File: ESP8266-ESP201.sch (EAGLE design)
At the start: 17 parts

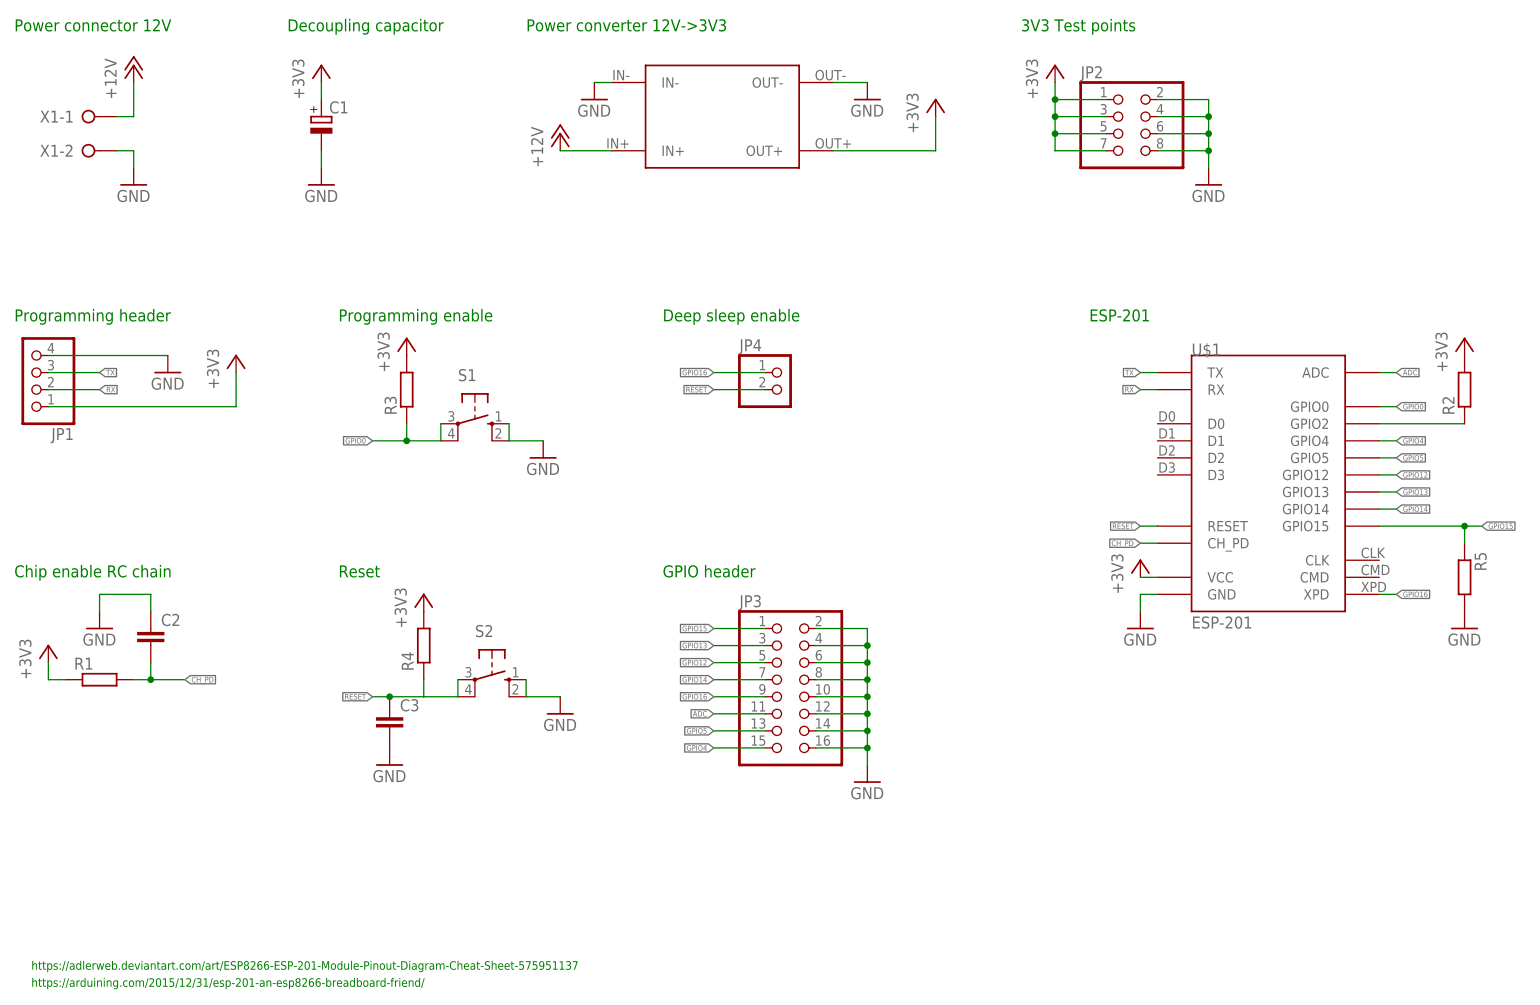
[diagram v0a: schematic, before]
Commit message: New version of the board with proper mounting holes and smaller footprint
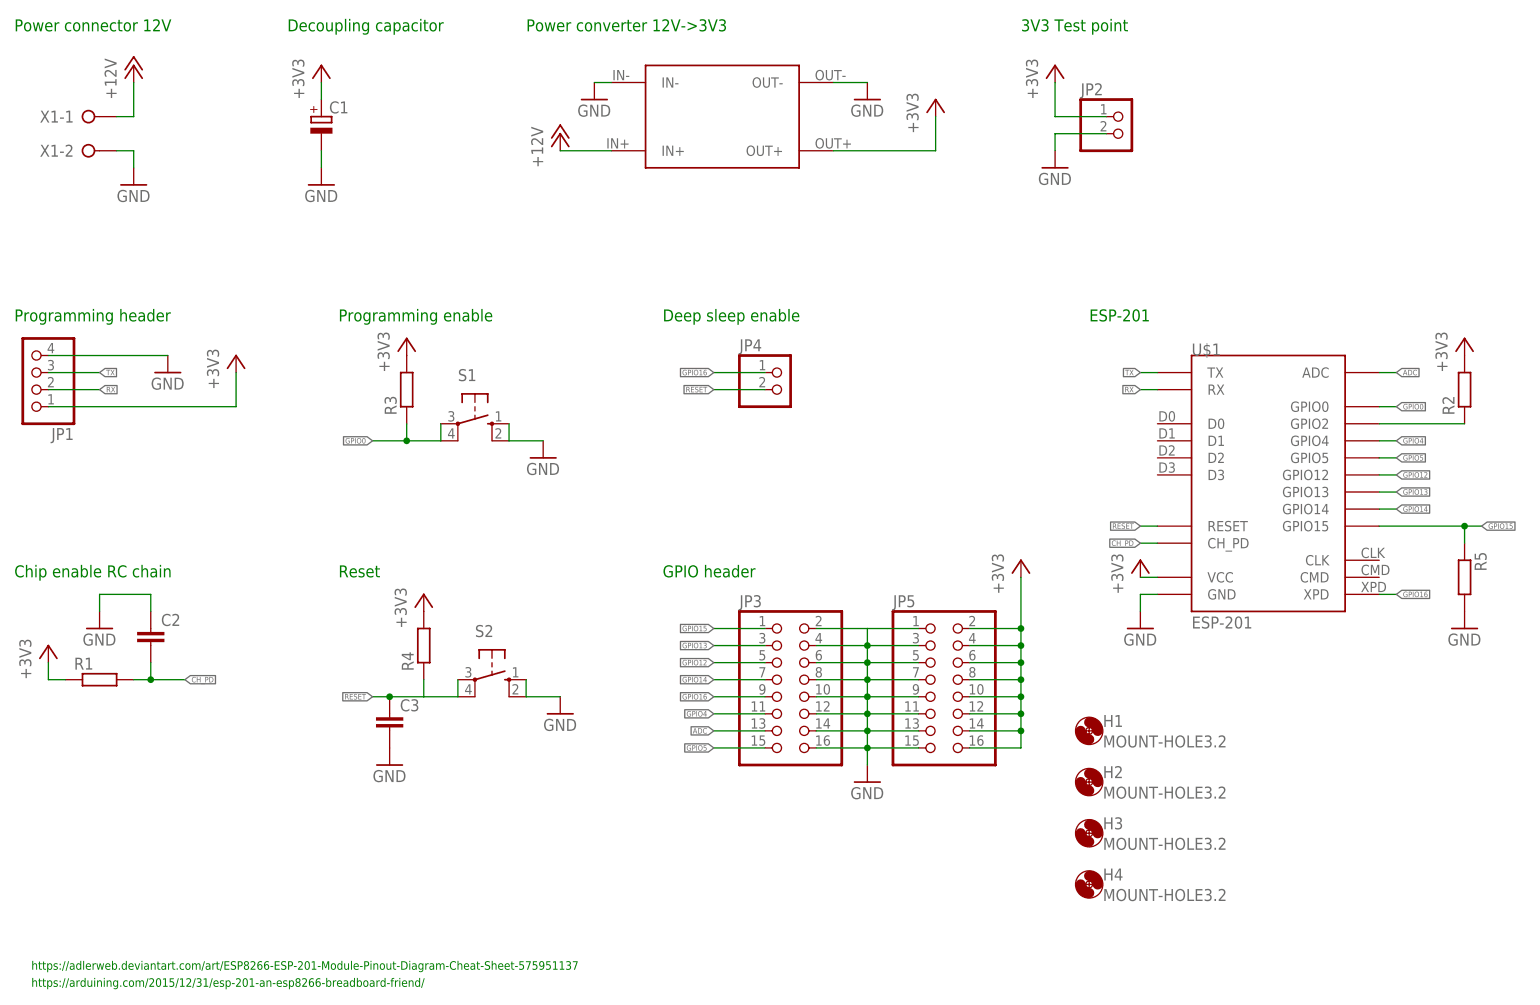
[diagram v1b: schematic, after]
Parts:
- added H1, H2, H3, H4: MOUNT-HOLE3.2, holes:MOUNT-HOLE3.2
- added JP5: (no value), pinhead:PINHD-2X8
- JP2: device pinhead:PINHD-2X4 -> pinhead:PINHD-1X2
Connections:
- net +3V3: now also JP5.10, JP5.12, JP5.14, JP5.16, JP5.2, JP5.4, JP5.6, JP5.8; no longer JP2.3, JP2.5, JP2.7
- net ADC: now also JP3.13; no longer JP3.11
- net GND: now also JP5.1, JP5.11, JP5.13, JP5.15, JP5.3, JP5.5, JP5.7, JP5.9; no longer JP2.4, JP2.6, JP2.8
- net GPIO4: now also JP3.11; no longer JP3.15
- net GPIO5: now also JP3.15; no longer JP3.13
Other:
- note added: "3V3 Test point"
- note removed: "3V3 Test points"

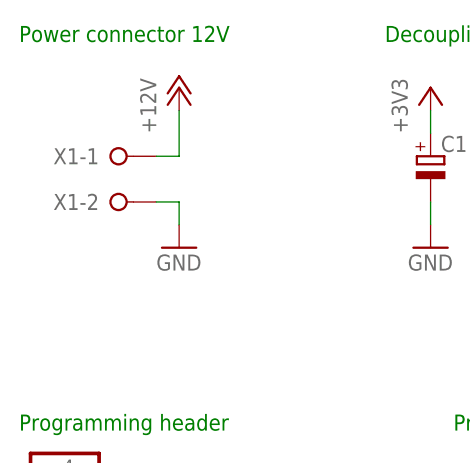
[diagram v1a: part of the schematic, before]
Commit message: More compact layout and added bottom silk screen
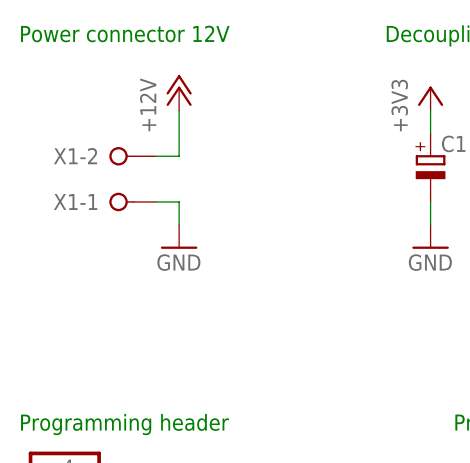
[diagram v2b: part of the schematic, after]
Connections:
- net +12V: now also X1-2.KL; no longer X1-1.KL
- net GND: now also X1-1.KL; no longer X1-2.KL
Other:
- moved on the sheet: X1-1, X1-2
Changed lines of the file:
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@@
 <?xml version="1.0" encoding="utf-8"?>
 <!DOCTYPE eagle SYSTEM "eagle.dtd">
-<eagle version="6.6.0">
+<eagle version="7.6.0">
 <drawing>
 <settings>
@@
 <instance part="P+2" gate="1" x="33.02" y="154.94"/>
 <instance part="GND5" gate="1" x="33.02" y="137.16"/>
-<instance part="X1" gate="-1" x="25.4" y="147.32"/>
-<instance part="X1" gate="-2" x="25.4" y="142.24"/>
+<instance part="X1" gate="-1" x="25.4" y="142.24"/>
+<instance part="X1" gate="-2" x="25.4" y="147.32"/>
 <instance part="R1" gate="G$1" x="27.94" y="63.5"/>
 <instance part="+3V1" gate="G$1" x="20.32" y="68.58"/>
@@
 </segment>
 <segment>
-<pinref part="X1" gate="-2" pin="KL"/>
 <pinref part="GND5" gate="1" pin="GND"/>
+<wire x1="33.02" y1="142.24" x2="33.02" y2="139.7" width="0.1524" layer="91"/>
+<pinref part="X1" gate="-1" pin="KL"/>
 <wire x1="30.48" y1="142.24" x2="33.02" y2="142.24" width="0.1524" layer="91"/>
-<wire x1="33.02" y1="142.24" x2="33.02" y2="139.7" width="0.1524" layer="91"/>
 </segment>
 <segment>
@@
 </segment>
 <segment>
-<pinref part="X1" gate="-1" pin="KL"/>
 <pinref part="P+2" gate="1" pin="+12V"/>
+<wire x1="33.02" y1="147.32" x2="33.02" y2="152.4" width="0.1524" layer="91"/>
+<pinref part="X1" gate="-2" pin="KL"/>
 <wire x1="30.48" y1="147.32" x2="33.02" y2="147.32" width="0.1524" layer="91"/>
-<wire x1="33.02" y1="147.32" x2="33.02" y2="152.4" width="0.1524" layer="91"/>
 </segment>
 </net>

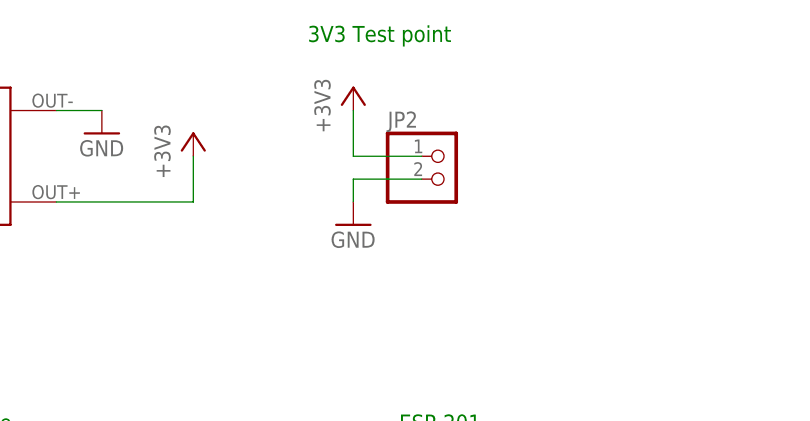
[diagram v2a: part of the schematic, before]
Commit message: Removed 3V3 test point
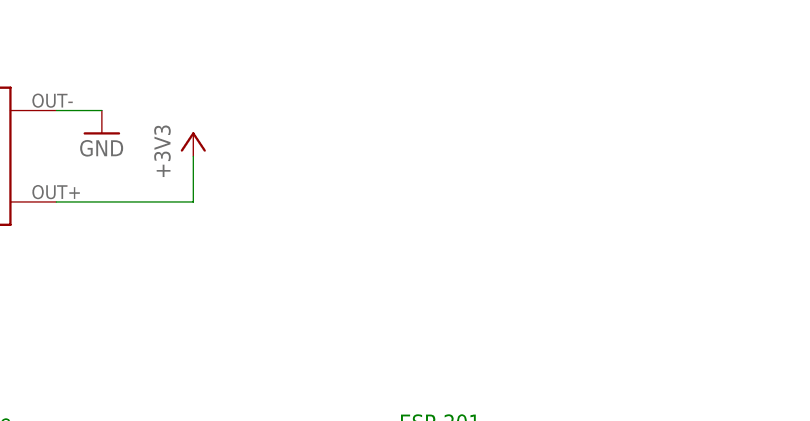
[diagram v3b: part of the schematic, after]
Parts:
- removed JP2: (no value), pinhead:PINHD-1X2
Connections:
- net +3V3: no longer JP2.1
- net GND: no longer JP2.2
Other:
- note removed: "3V3 Test point"
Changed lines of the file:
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@@
 <part name="H3" library="holes" deviceset="MOUNT-HOLE" device="3.2"/>
 <part name="H4" library="holes" deviceset="MOUNT-HOLE" device="3.2"/>
-<part name="JP2" library="pinhead" deviceset="PINHD-1X2" device=""/>
-<part name="+3V7" library="supply1" deviceset="+3V3" device=""/>
-<part name="GND9" library="supply1" deviceset="GND" device=""/>
 <part name="JP5" library="pinhead" deviceset="PINHD-2X8" device=""/>
 <part name="+3V10" library="supply1" deviceset="+3V3" device=""/>
@@
 <text x="63.5" y="116.84" size="1.778" layer="91">Programming enable</text>
 <text x="175.26" y="116.84" size="1.778" layer="91">ESP-201</text>
-<text x="165.1" y="160.02" size="1.778" layer="91">3V3 Test point</text>
 <text x="111.76" y="78.74" size="1.778" layer="91">GPIO header</text>
 <text x="63.5" y="78.74" size="1.778" layer="91">Reset</text>
@@
 <instance part="H3" gate="G$1" x="175.26" y="40.64"/>
 <instance part="H4" gate="G$1" x="175.26" y="33.02"/>
-<instance part="JP2" gate="G$1" x="180.34" y="144.78"/>
-<instance part="+3V7" gate="G$1" x="170.18" y="154.94"/>
-<instance part="GND9" gate="1" x="170.18" y="139.7"/>
 <instance part="JP5" gate="A" x="152.4" y="63.5"/>
 <instance part="+3V10" gate="G$1" x="165.1" y="81.28"/>
@@
 <pinref part="GND13" gate="1" pin="GND"/>
 </segment>
-<segment>
-<pinref part="JP2" gate="G$1" pin="2"/>
-<wire x1="177.8" y1="144.78" x2="170.18" y2="144.78" width="0.1524" layer="91"/>
-<wire x1="170.18" y1="144.78" x2="170.18" y2="142.24" width="0.1524" layer="91"/>
-<pinref part="GND9" gate="1" pin="GND"/>
-</segment>
 </net>
 <net name="+12V" class="0">
@@
 </segment>
 <segment>
-<pinref part="JP2" gate="G$1" pin="1"/>
-<wire x1="177.8" y1="147.32" x2="170.18" y2="147.32" width="0.1524" layer="91"/>
-<wire x1="170.18" y1="147.32" x2="170.18" y2="152.4" width="0.1524" layer="91"/>
-<pinref part="+3V7" gate="G$1" pin="+3V3"/>
-</segment>
-<segment>
